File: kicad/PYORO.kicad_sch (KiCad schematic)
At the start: 34 parts, among them J1 BM06B-SRSS-TBLFSN, J2 Conn_01x04_Pin, J3 BM06B-SRSS-TBLFSN, Q1 TEFT4300, Q2 TEFT4300, Q3 TEFT4300, Q4 TEFT4300, U1 STM32H503CBTx, U2 L293D, U3 ICM-20948

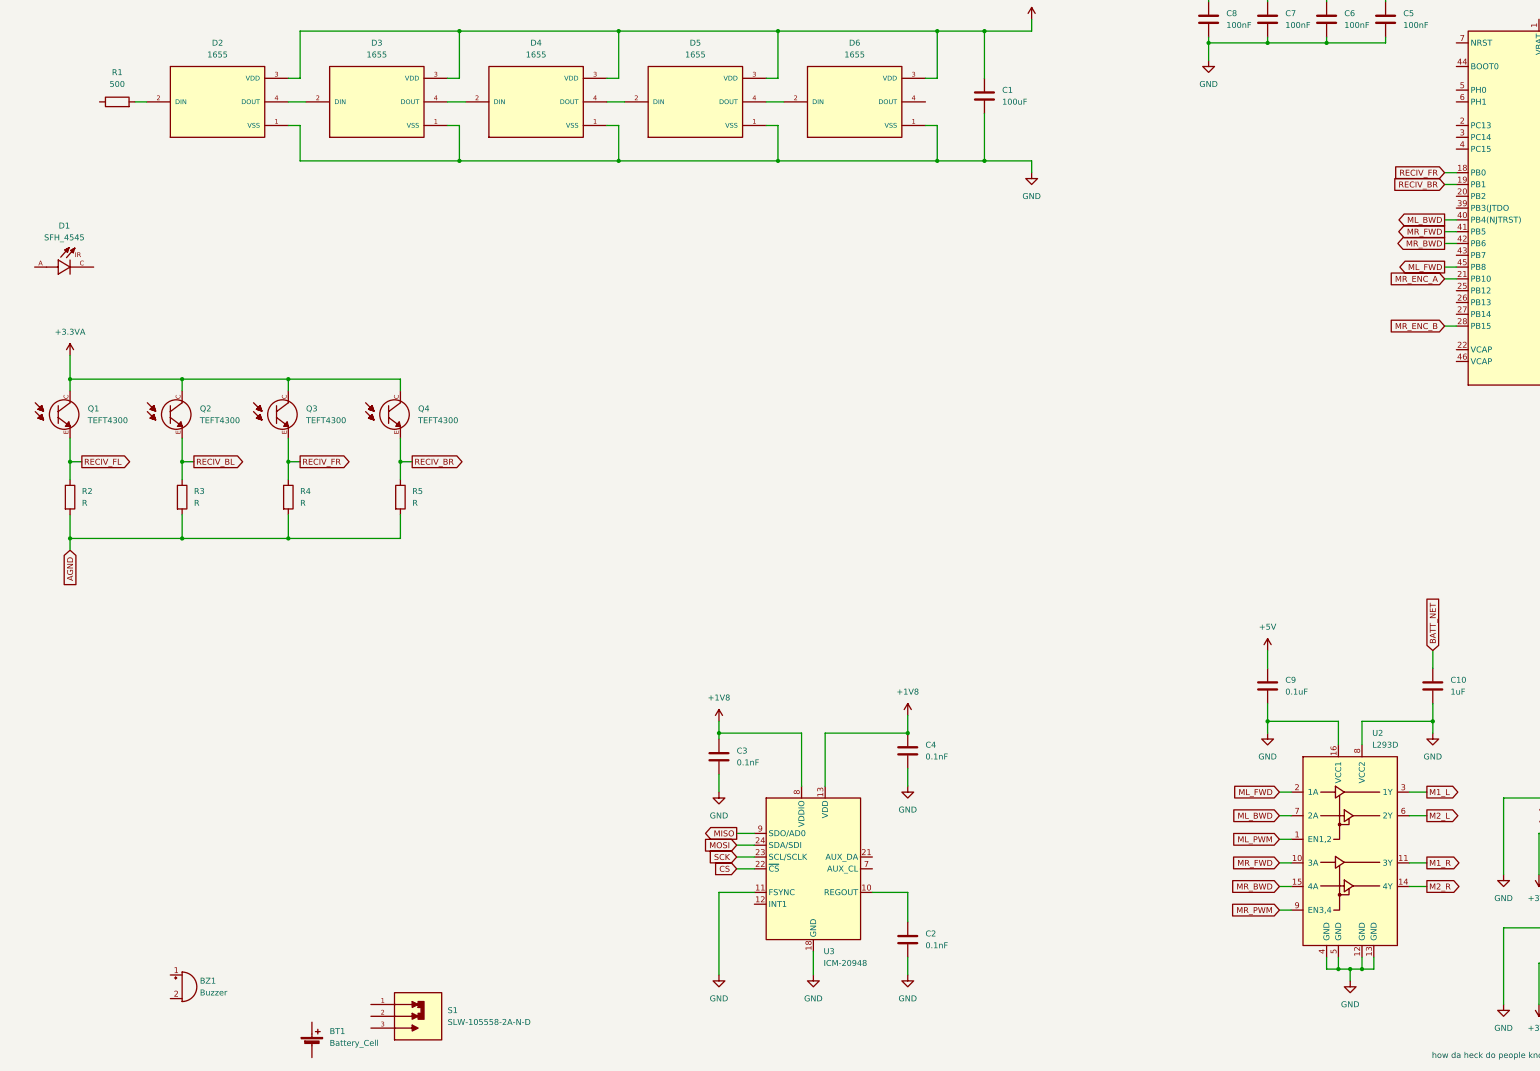
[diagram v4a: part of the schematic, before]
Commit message: Started IR Emitters, and enable MCU flash
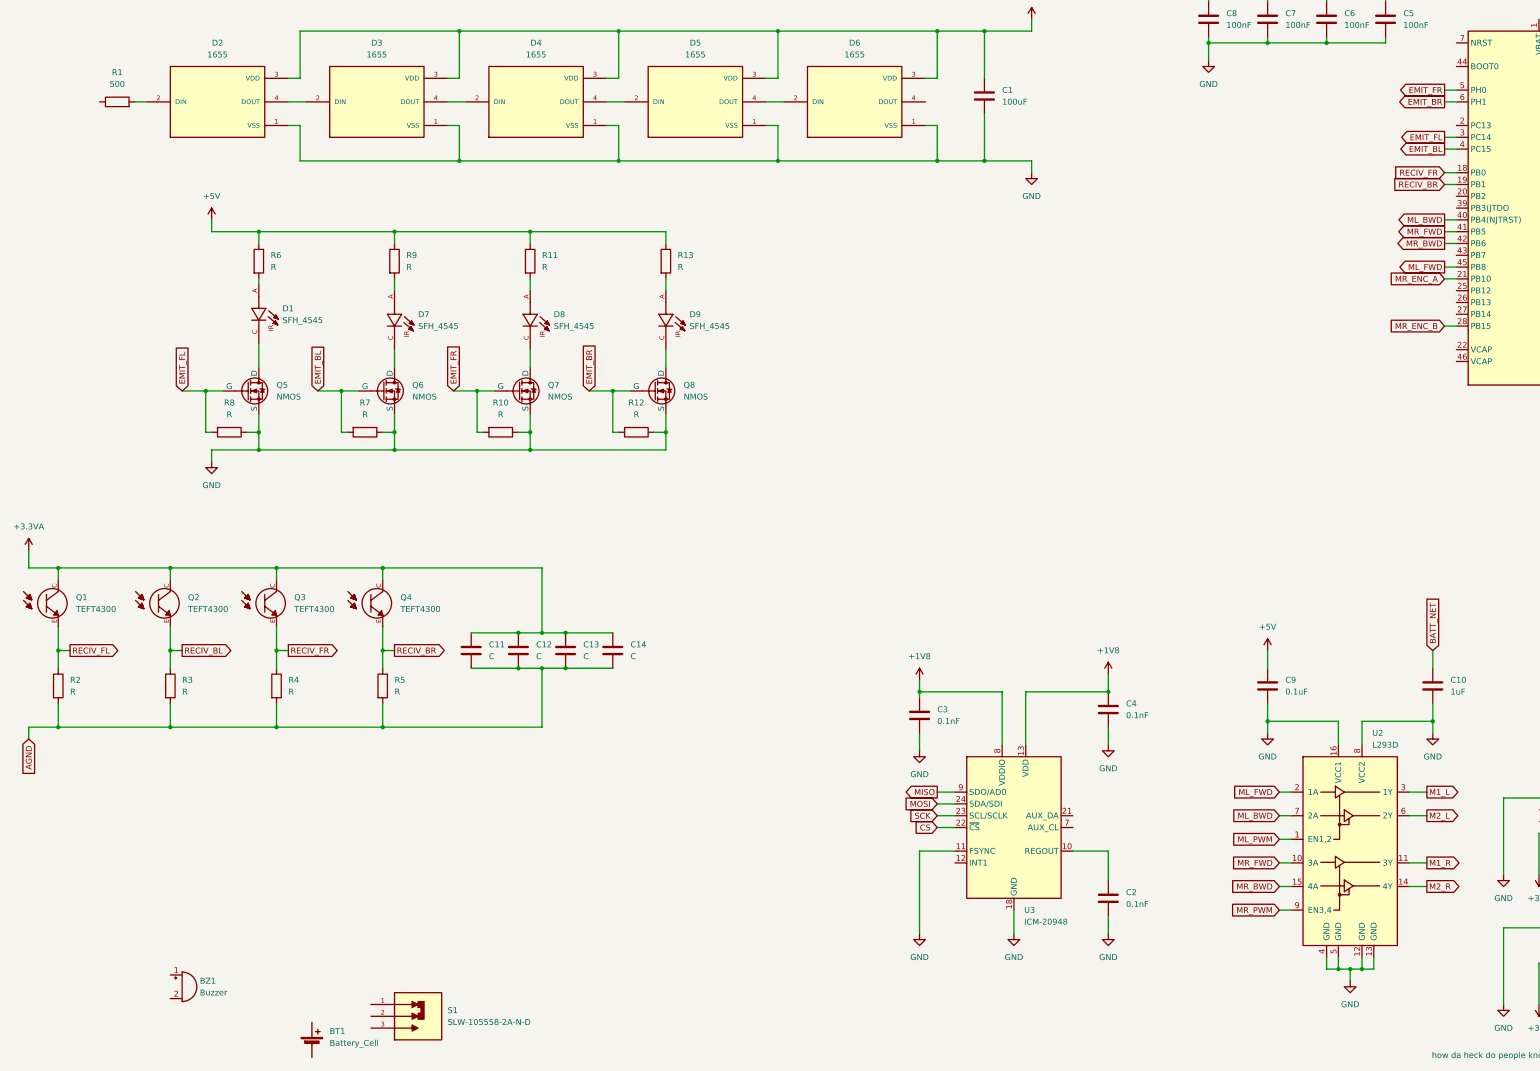
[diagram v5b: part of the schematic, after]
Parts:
- added C11, C12, C13, C14: C, symbol Device:C
- added D7, D8, D9: SFH_4545, MM_Library:Emitter, symbol SFH_4545:SFH_4545
- added Q5, Q6, Q7, Q8: NMOS, symbol Simulation_SPICE:NMOS
- added R10, R11, R12, R13, R6, R7, R8, R9: R, symbol Device:R
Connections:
- net +3.3VA: now also C11.1, C12.1, C13.1, C14.1
- net +5V: now also R11.1, R13.1, R6.1, R9.1
- net AGND: now also C11.2, C12.2, C13.2, C14.2
- net GND: now also Q5.3 (S), Q6.3 (S), Q7.3 (S), Q8.3 (S), R10.1, R12.1, R7.1, R8.1
- net EMIT_FL: now reaches U1.3 (PC14)
- net EMIT_FL: now also Q5.2 (G), R8.2
- net EMIT_BL: now reaches U1.4 (PC15)
- net EMIT_BL: now also Q6.2 (G), R7.2
- net EMIT_FR: now reaches U1.5 (PH0)
- net EMIT_FR: now also Q7.2 (G), R10.2
- net EMIT_BR: now reaches U1.6 (PH1)
- net EMIT_BR: now also Q8.2 (G), R12.2
- net at D1.A: now also R6.2
- net at D1.C: now also Q5.1 (D)
- new net: D7.A, R9.2
- new net: D9.A, R13.2
- new net: D8.C, Q7.1 (D)
- new net: D7.C, Q6.1 (D)
- new net: D8.A, R11.2
- new net: D9.C, Q8.1 (D)
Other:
- moved on the sheet: C2, C3, C4, D1, Q1, Q2, Q3, Q4, R2, R3, R4, R5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

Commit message: Started Buzzer
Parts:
- added C15, C16: 0.1uF, symbol Device:C
- added Q9: NMOS, symbol Simulation_SPICE:NMOS
- added R14, R15: R, symbol Device:R
- added TP1, TP2: TestPoint, symbol Connector:TestPoint
- added U4: MC78LC18NTR, Package_TO_SOT_SMD:SOT-23-5, symbol Regulator_Linear:MC78LC18NTR
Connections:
- net +1V8: now also C16.1, TP2.1, U4.3 (Vout)
- net +5V: now also BZ1.1 (+), R14.1
- net GND: now also BT1.2 (-), C15.2, C16.2, Q9.3 (S), R15.2, U4.1 (GND)
- net at BT1.1 (+): now also S1.1
- net BUZZER_PWM: now reaches U1.32 (PA11)
- net BUZZER_PWM: now also Q9.2 (G), R15.1
- net at BZ1.2 (-): now also Q9.1 (D), R14.2
- net at S1.3: now also TP1.1
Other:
- moved on the sheet: BT1, BZ1, S1

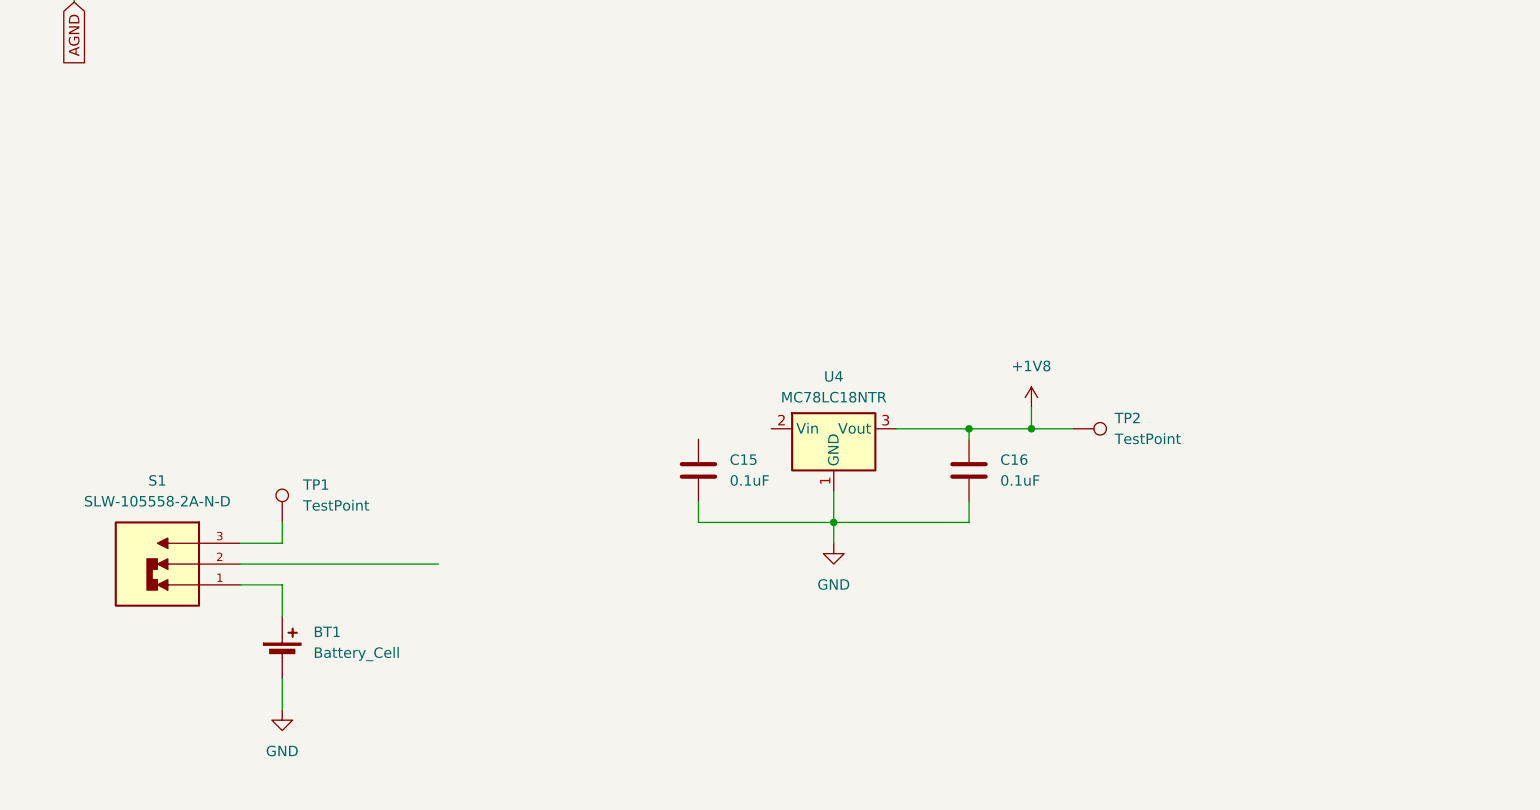
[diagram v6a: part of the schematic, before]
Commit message: Started voltage regulators
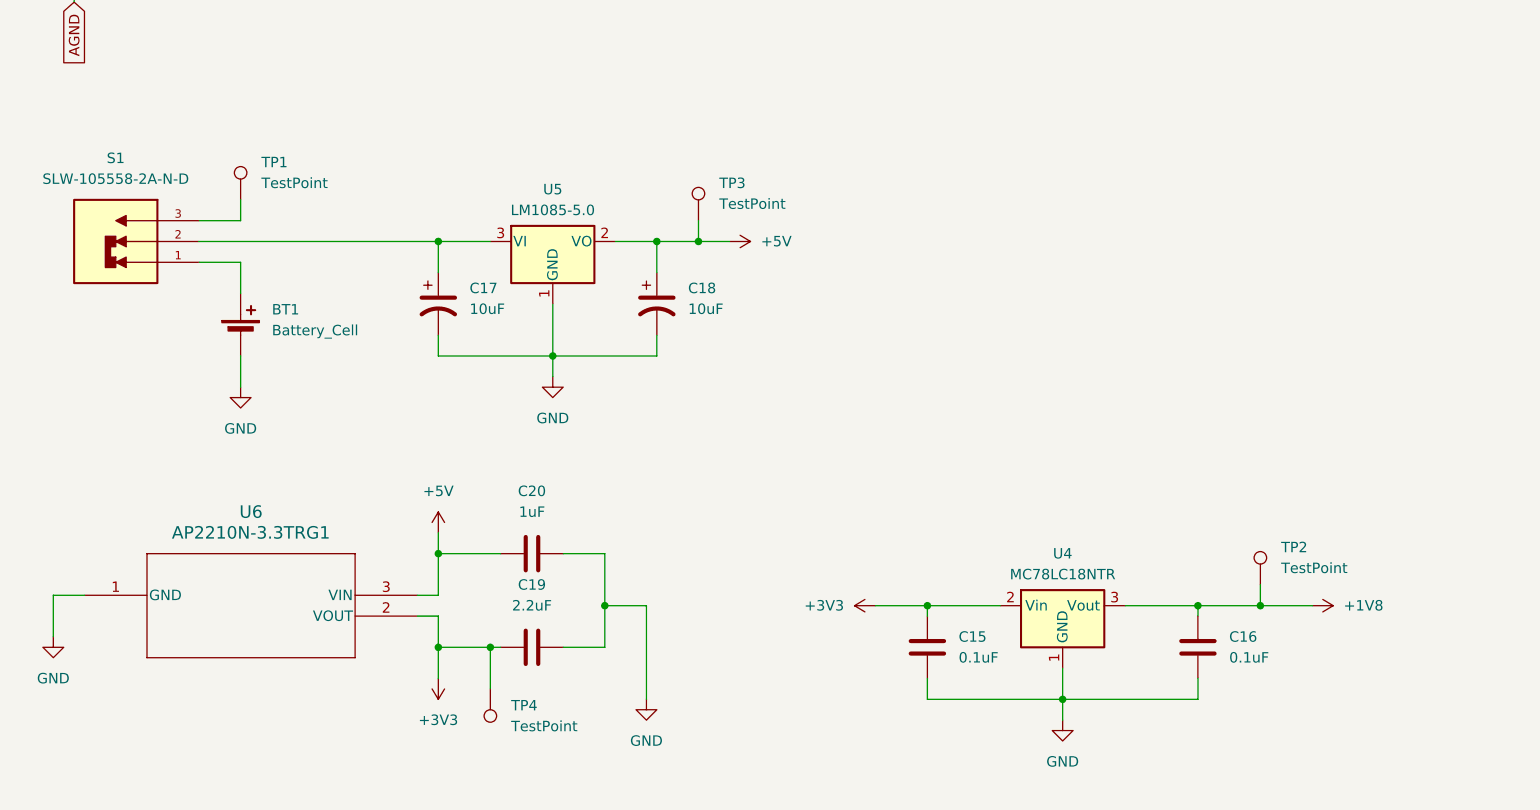
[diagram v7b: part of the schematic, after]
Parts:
- added C17, C18: 10uF, symbol Device:C_Polarized_US
- added C19: 2.2uF, symbol Device:C
- added C20: 1uF, symbol Device:C
- added TP3, TP4: TestPoint, symbol Connector:TestPoint
- added U5: LM1085-5.0, symbol Regulator_Linear:LM1085-5.0
- added U6: AP2210N-3.3TRG1, Package_TO_SOT_SMD:SOT-23W, symbol 2025-08-04_04-37-33:AP2210N-3.3TRG1
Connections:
- net +3V3: now also C15.1, U4.2 (Vin), C19.1, TP4.1, U6.2 (VOUT)
- net +5V: now also C18.1, C20.1, TP3.1, U5.2 (VO), U6.3 (VIN)
- net GND: now also C17.2, C18.2, C19.2, C20.2, U5.1 (GND), U6.1 (GND)
- net at S1.2: now also C17.1, U5.3 (VI)
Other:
- moved on the sheet: BT1, C15, C16, S1, TP1, TP2, U4

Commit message: Added Neopixel PWM pin, and reoganized schematic
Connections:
- net NEOPXL_PWM: now reaches U1.30 (PA9)
- net NEOPXL_PWM: now also R1.1
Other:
- moved on the sheet: BT1, BZ1, C1, C10, C11, C12, C13, C14, C15, C16, C17, C18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
